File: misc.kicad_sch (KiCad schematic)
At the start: 24 parts, among them U2 NTS0102_TSSOP, U3 NTS0102_TSSOP, Y1 Oscillator_25MHz_511ABA25M000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, Y2 Resonator_50MHz_XRCGE

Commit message: [#81595] Update symbols from library
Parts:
- Y1: Manufacturer Skyworks -> Skyworks Solutions
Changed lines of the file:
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@@
 			)
 		)
-		(property "Datasheet" "https://www.mouser.pl/datasheet/2/472/si510_11-2507765.pdf"
+		(property "Datasheet" "https://www.mouser.com/datasheet/2/472/si510_11-2507765.pdf"
 			(at 296.545 85.725 0)
 			(effects
@@
 			)
 		)
-		(property "Manufacturer" "Skyworks"
+		(property "Manufacturer" "Skyworks Solutions"
 			(at 296.545 73.025 0)
 			(effects

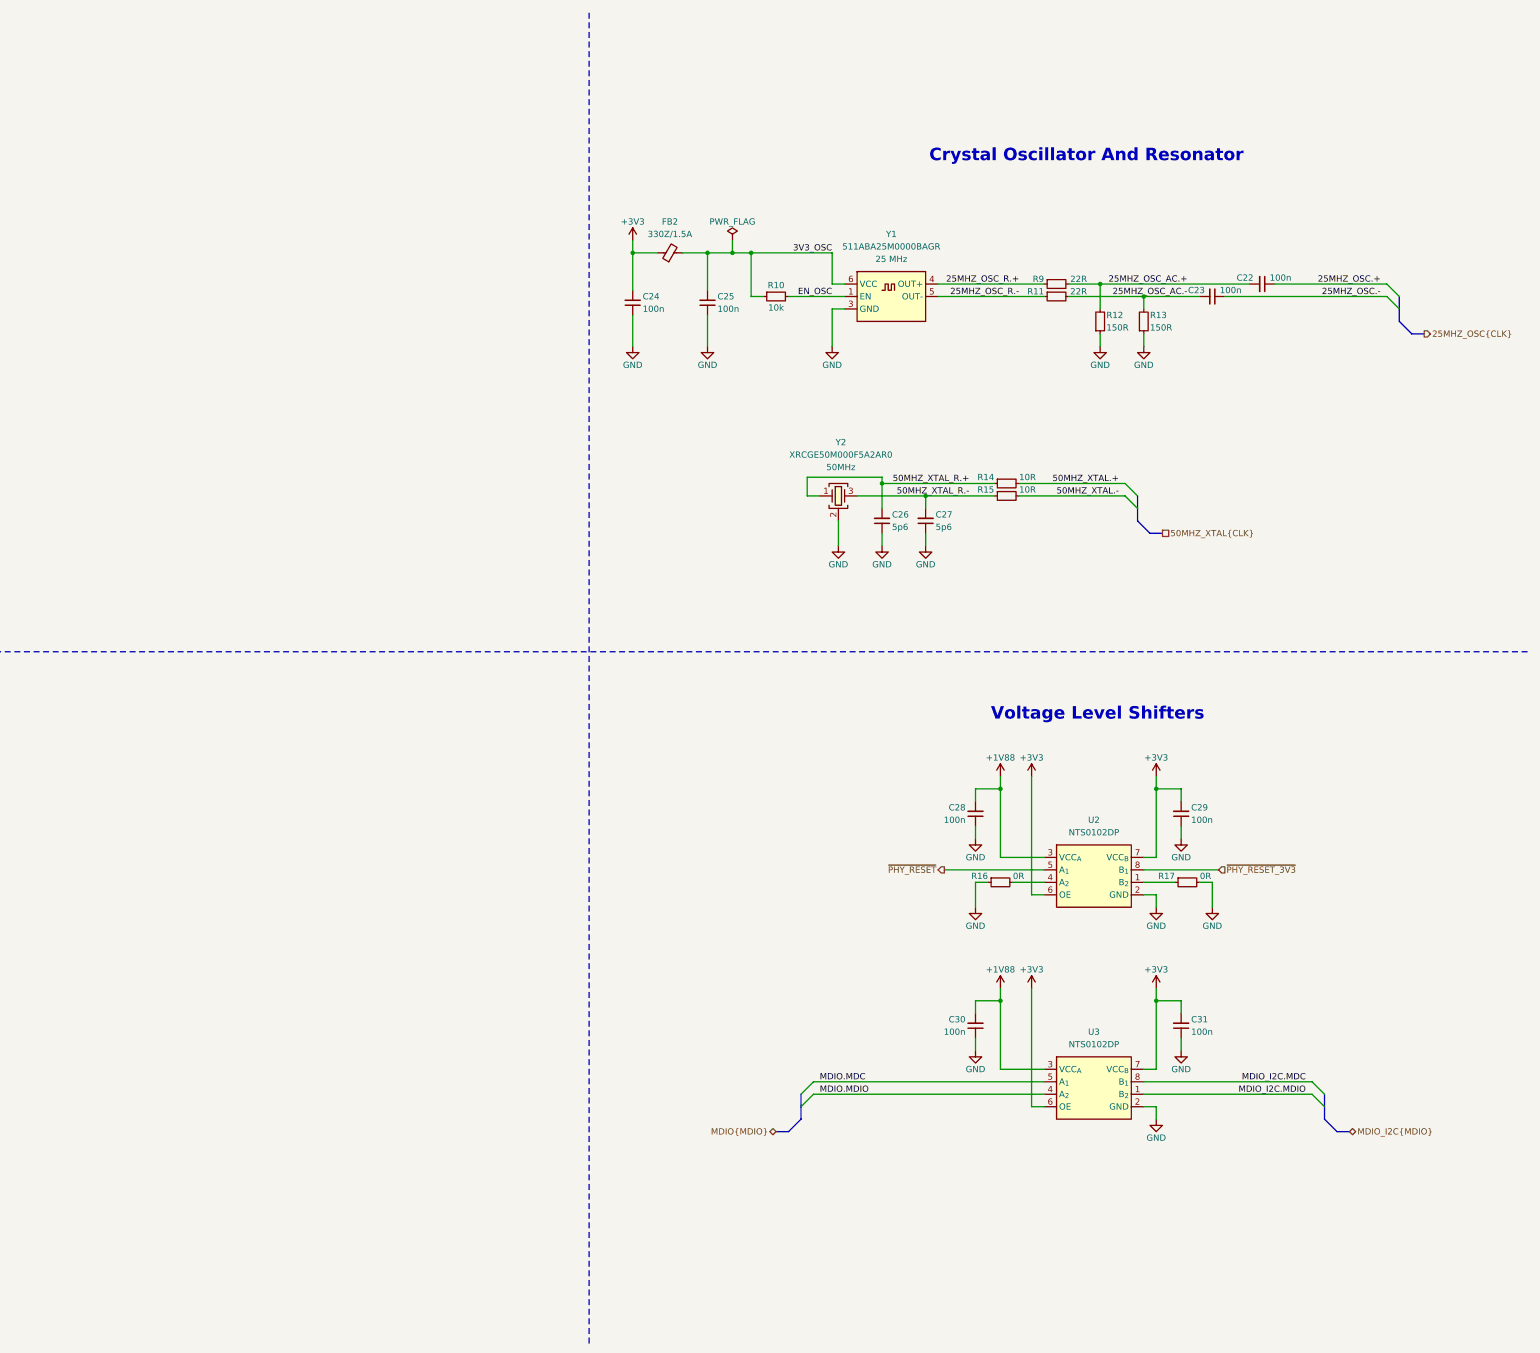
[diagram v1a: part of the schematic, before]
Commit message: [#85196] Change 2u2 inductor, minor schematic cleanup
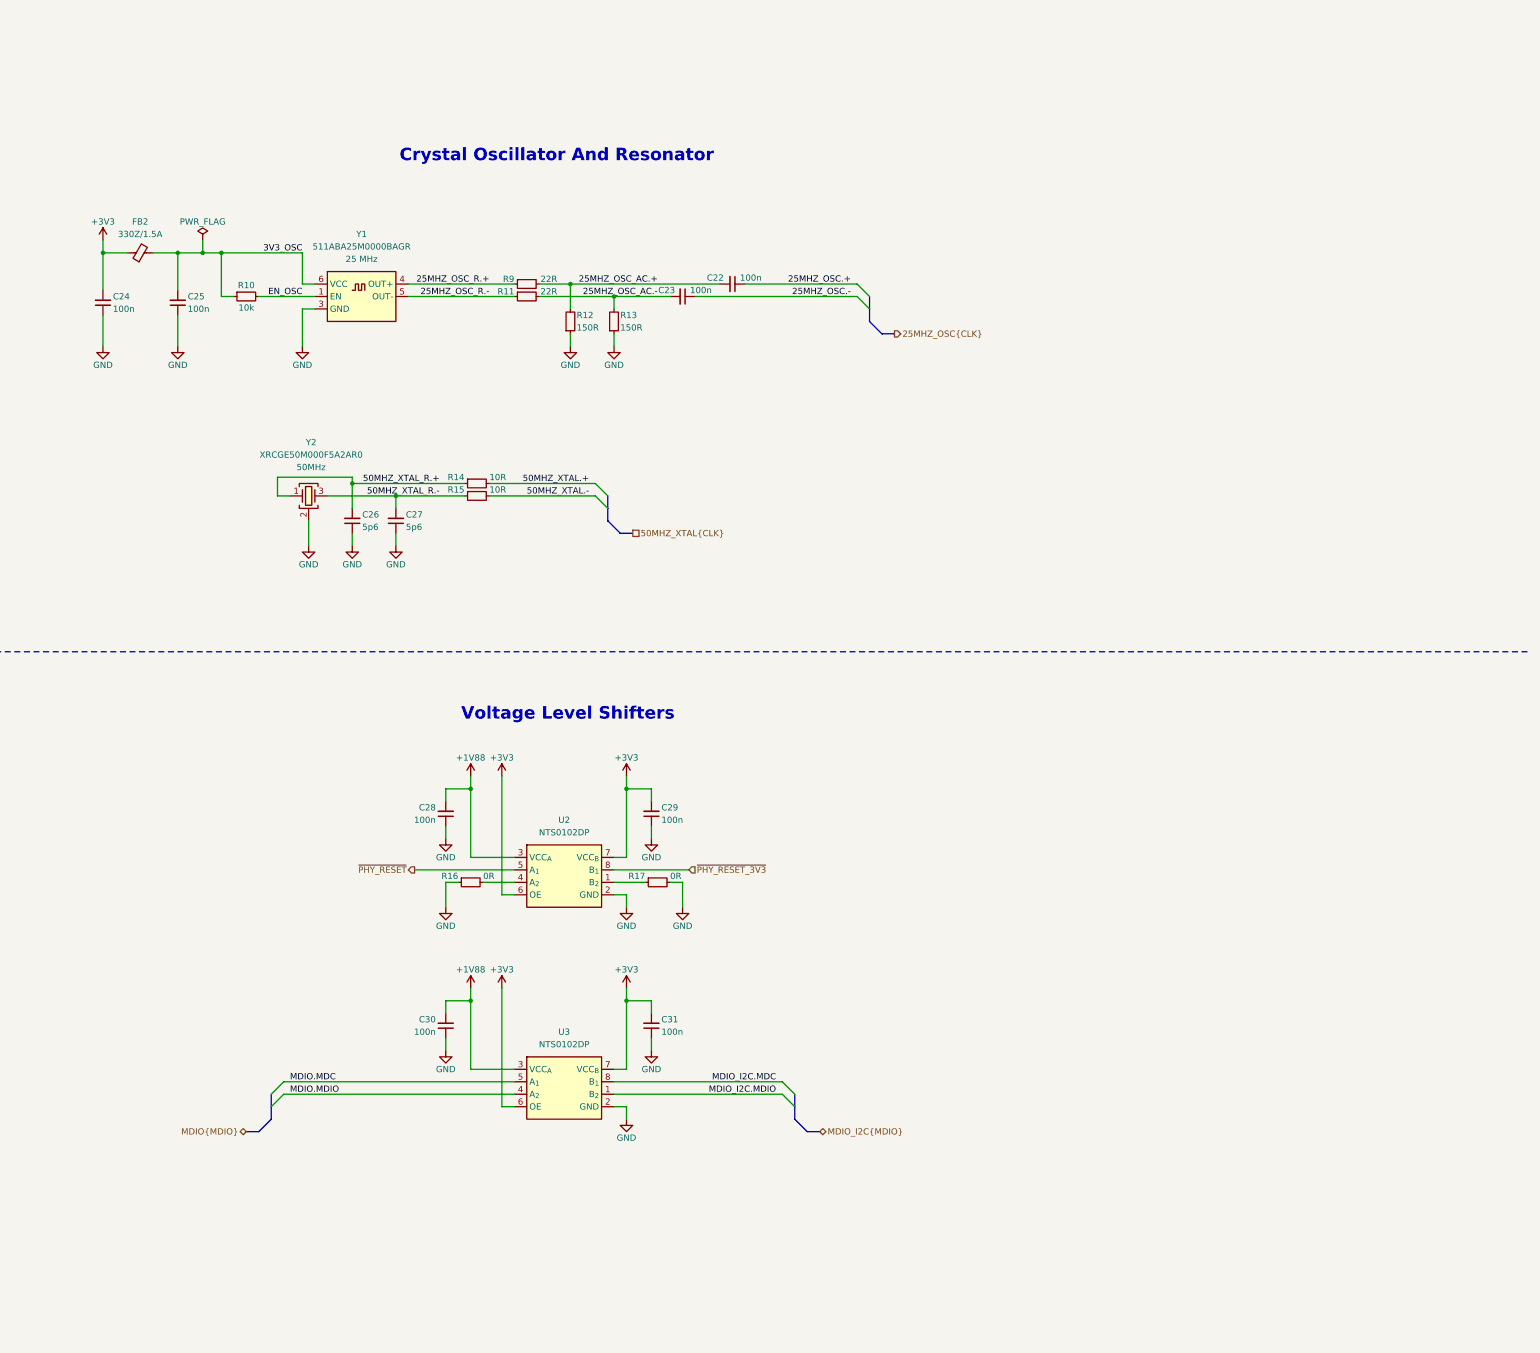
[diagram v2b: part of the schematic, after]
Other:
- moved on the sheet: C22, C23, C24, C25, C26, C27, C28, C29, C30, C31, FB2, R10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

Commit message: [#85196] Re-annotate schematic
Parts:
- renumbered C22 to C68, C23 to C69, C24 to C70, C25 to C71, C26 to C72, C27 to C73, C28 to C74, C29 to C75, C30 to C76, C31 to C77, R9 to R42, R10 to R43, R11 to R44, R12 to R45, R13 to R46, R14 to R47, R15 to R48, R16 to R49, R17 to R50, U2 to U7, U3 to U8
